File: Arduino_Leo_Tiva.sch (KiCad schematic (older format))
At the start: 53 parts, among them J1 USB_OTG, J10 Digital, J11 TDI, J12 TDO, J13 TXD, J14 RXD, J15 -AREF, J16 +AREF, J17 SPI 2 (D6,D7), J18 SERIAL 3, 4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

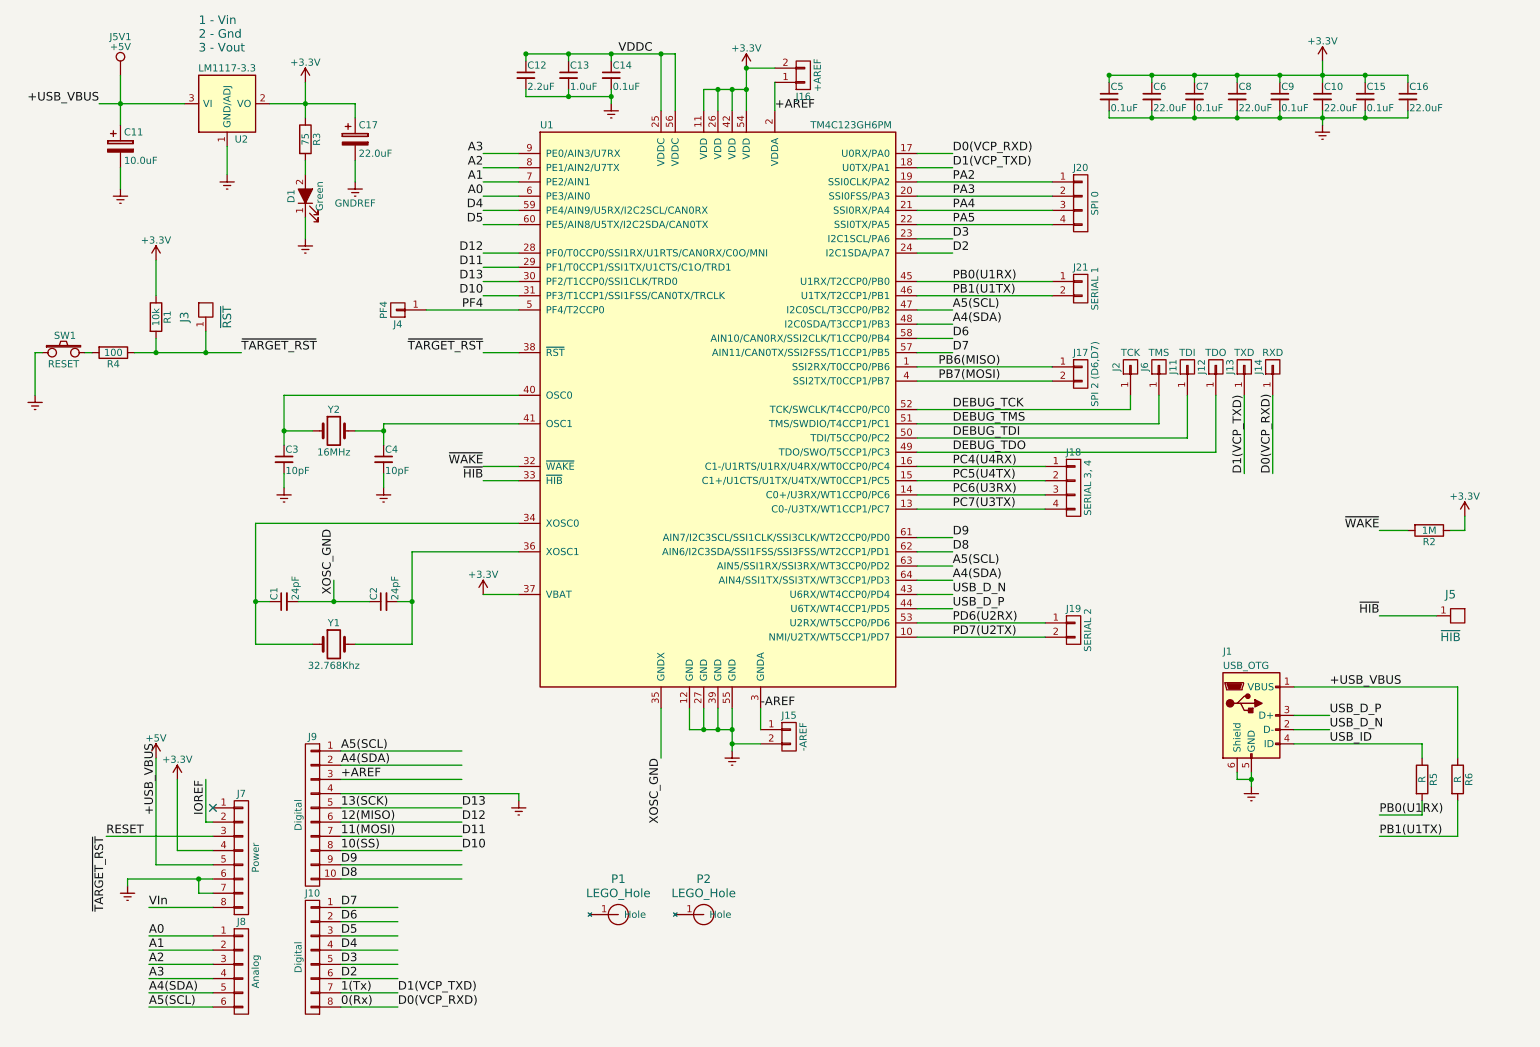
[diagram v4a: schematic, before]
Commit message: Major changes to board layout and design leading towards revisoin v1.1
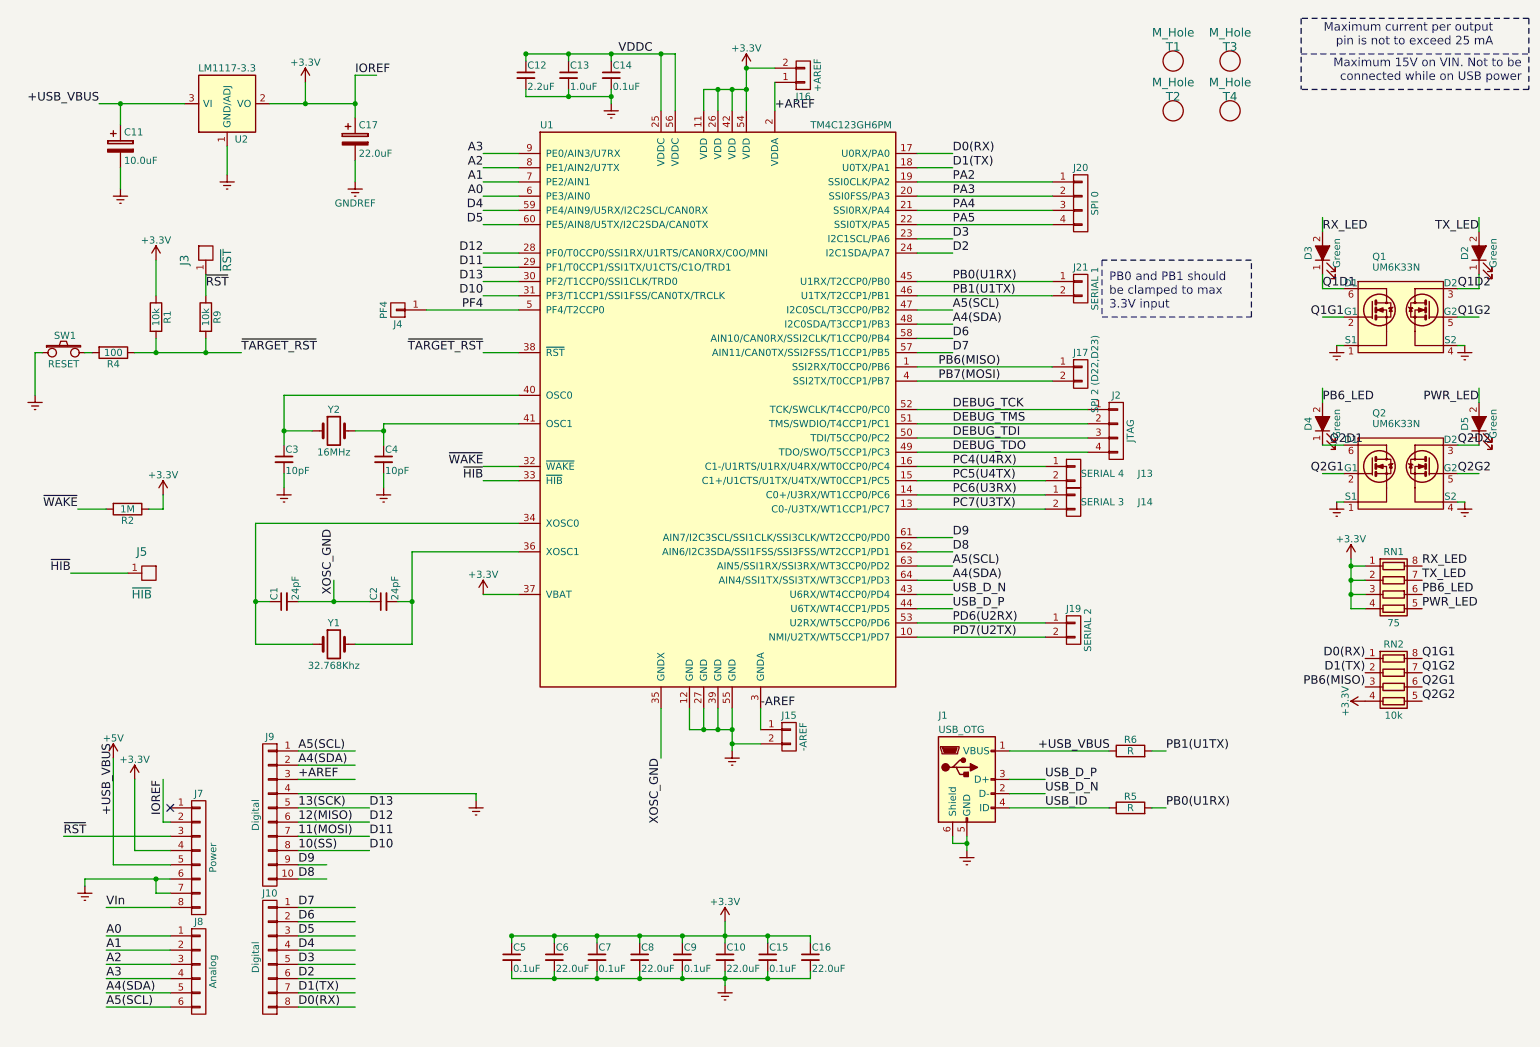
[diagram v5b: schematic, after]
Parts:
- removed D1: Green, LEDs:LED_0805, symbol LED_ALT
- removed J11: TDI, Pin_Headers:Pin_Header_Straight_1x01_Pitch2.54mm, symbol CONN_01X01
- removed J12: TDO, Pin_Headers:Pin_Header_Straight_1x01_Pitch2.54mm, symbol CONN_01X01
- removed J13: TXD, Pin_Headers:Pin_Header_Straight_1x01_Pitch2.54mm, symbol CONN_01X01
- removed J14: RXD, Pin_Headers:Pin_Header_Straight_1x01_Pitch2.54mm, symbol CONN_01X01
- removed J18: SERIAL 3, 4, Socket_Strips:Socket_Strip_Straight_1x04_Pitch2.54mm, symbol CONN_01X04
- removed J2: TCK, Pin_Headers:Pin_Header_Straight_1x01_Pitch2.54mm, symbol CONN_01X01
- removed J5V1: +5V, Pin_Headers:Pin_Header_Straight_1x01_Pitch2.54mm, symbol TEST_1P
- removed J6: TMS, Pin_Headers:Pin_Header_Straight_1x01_Pitch2.54mm, symbol CONN_01X01
- removed P1, P2: LEGO_Hole, Custom-Mounting-Holes:Lego-Hole, symbol LEGO_Hole
- removed R3: 75, Resistors_SMD:R_0603, symbol R
- added D2, D3, D4, D5: Green, LEDs:LED_0805_HandSoldering, symbol LED_ALT
- added J13: SERIAL 4, Socket_Strips:Socket_Strip_Straight_1x02_Pitch2.54mm, symbol CONN_01X02
- added J14: SERIAL 3, Socket_Strips:Socket_Strip_Straight_1x02_Pitch2.54mm, symbol CONN_01X02
- added J2: JTAG, Connectors_Local:Pin_Header_Straight_2x02_Pitch2.54mm, symbol CONN_01X04
- added Q1, Q2: UM6K33N, TO_SOT_Packages_SMD_Local:SOT-363_SC-70-6_Handsoldering, symbol UM6K33N
- added R9: 10k, Resistors_SMD:R_0603_HandSoldering, symbol R
- added RN1: 75, Project-Symbols_Local:YC164-JR-0775RL, symbol R_Pack04
- added RN2: 10k, Project-Symbols_Local:CRA12E08310K0JTR, symbol R_Pack04
- added T1, T2, T3, T4: M_Hole, Custom-Mounting-Holes:ArduinoMountingHole_3.2mm, symbol M_Hole
- J15, J16: footprint Pin_Headers:Pin_Header_Straight_1x02_Pitch2.54mm -> Custom-Mounting-Holes:NetTie-I_Connected_SMD
- J17: value SPI 2 (D6,D7) -> SPI 2 (D22,D23)
- J20: footprint Socket_Strips:Socket_Strip_Straight_1x04_Pitch2.54mm -> Socket_Strips:Socket_Strip_Straight_2x02_Pitch2.54mm
- J5: footprint Pin_Headers:Pin_Header_Straight_1x01_Pitch2.54mm -> Socket_Strips:Socket_Strip_Straight_1x01_Pitch2.54mm
- R1, R2, R4: footprint Resistors_SMD:R_0603 -> Resistors_SMD:R_0603_HandSoldering
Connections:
- net labels added: D0(RX), D1(TX), PB6_LED, PWR_LED, Q1D1, Q1D2, Q1G1, Q1G2, Q2D1, Q2D2, Q2G1, Q2G2, RX_LED, TX_LED, ~RST
- net labels removed: 0(Rx), 1(Tx), D0(VCP_RXD), D1(VCP_TXD), RESET
- wire segments 185 -> 199
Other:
- note added: "Maximum 15V on VIN. Not to be\nconnected while on USB power"
- note added: "Maximum current per output\npin is not to exceed 25 mA"
- note added: "PB0 and PB1 should \nbe clamped to max \n3.3V input"
- note removed: "1 - Vin\n2 - Gnd\n3 - Vout"
- moved on the sheet: C10, C15, C16, C5, C6, C7, C8, C9, J1, J10, J3, J5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

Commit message: Recent modifications to layout. Switching to resistor arrays. Adding Roadrunner image.
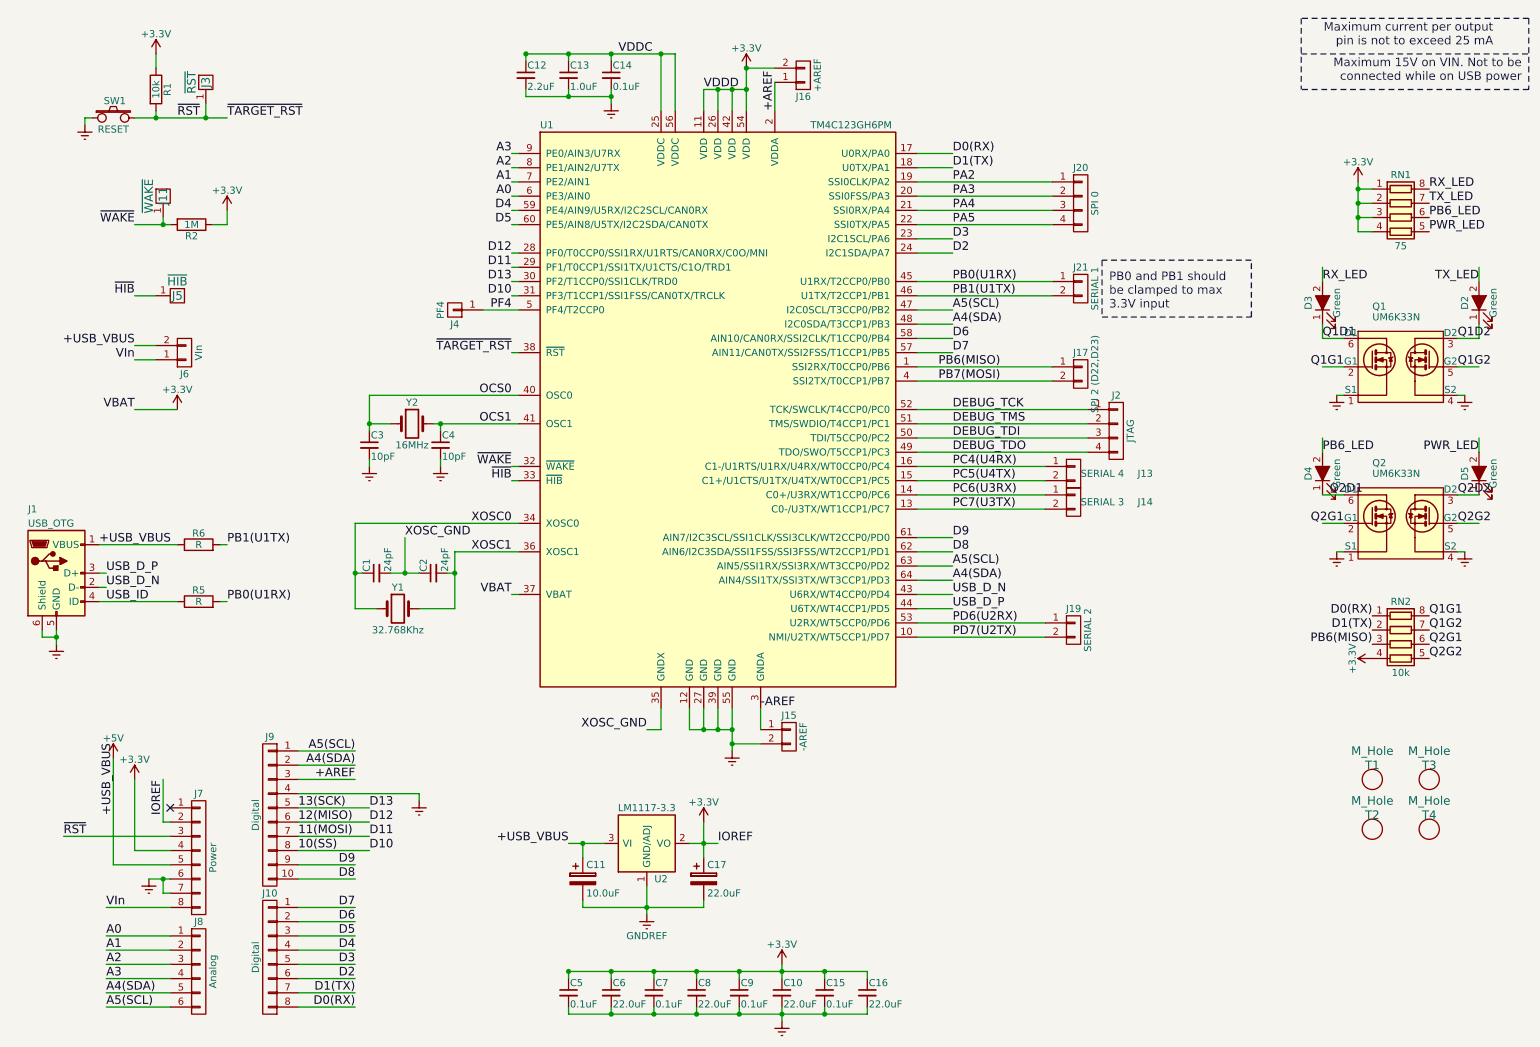
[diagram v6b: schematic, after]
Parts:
- removed R4: 100, Resistors_SMD:R_0603_HandSoldering, symbol R
- removed R9: 10k, Resistors_SMD:R_0603_HandSoldering, symbol R
- added J11: ~WAKE, Socket_Strips:Socket_Strip_Straight_1x01_Pitch2.54mm, symbol HEADER_1
- added J6: VIn, Custom-Mounting-Holes:NetTie-I_Connected_SMD, symbol CONN_01X02
- J2: footprint Connectors_Local:Pin_Header_Straight_2x02_Pitch2.54mm -> Pin_Headers:Pin_Header_Straight_2x02_Pitch2.54mm
- Q1, Q2: footprint TO_SOT_Packages_SMD_Local:SOT-363_SC-70-6_Handsoldering -> TO_SOT_Packages_SMD:SOT-363_SC-70-6_Handsoldering
- RN2: footprint Project-Symbols_Local:CRA12E08310K0JTR -> Project-Symbols_Local:YC164-JR-0775RL; Description RES ARRAY 4 RES 10K OHM 2012 -> RES ARRAY 4 RES 10K OHM 1206; Part # CRA12E08310K0JTR -> YC164-JR-0710KL
- U2: footprint TO_SOT_Packages_SMD_Local:SOT-223 -> TO_SOT_Packages_SMD:SOT-223
- Y1: footprint Crystals_Local:Crystal_DS26_d2.0mm_l6.0mm_Horizontal_1EP_style1 -> Project-Symbols_Local:Crystal_C26-LF_d2.1mm_l6.5mm_Horizontal_1EP_style1
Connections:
- net labels added: OCS0, OCS1, VBAT, VDDD, XOSC0, XOSC1
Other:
- moved on the sheet: C1, C10, C11, C15, C16, C17, C2, C3, C4, C5, C6, C7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
